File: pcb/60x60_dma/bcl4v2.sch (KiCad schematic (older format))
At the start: 31 parts, among them Q1 BSS138, SW1 SW_Push, SW2 SW_Push, SW3 SW_Push, U1 DS9166A-23, U2 STM32F070CBTx, Y1 Resonator

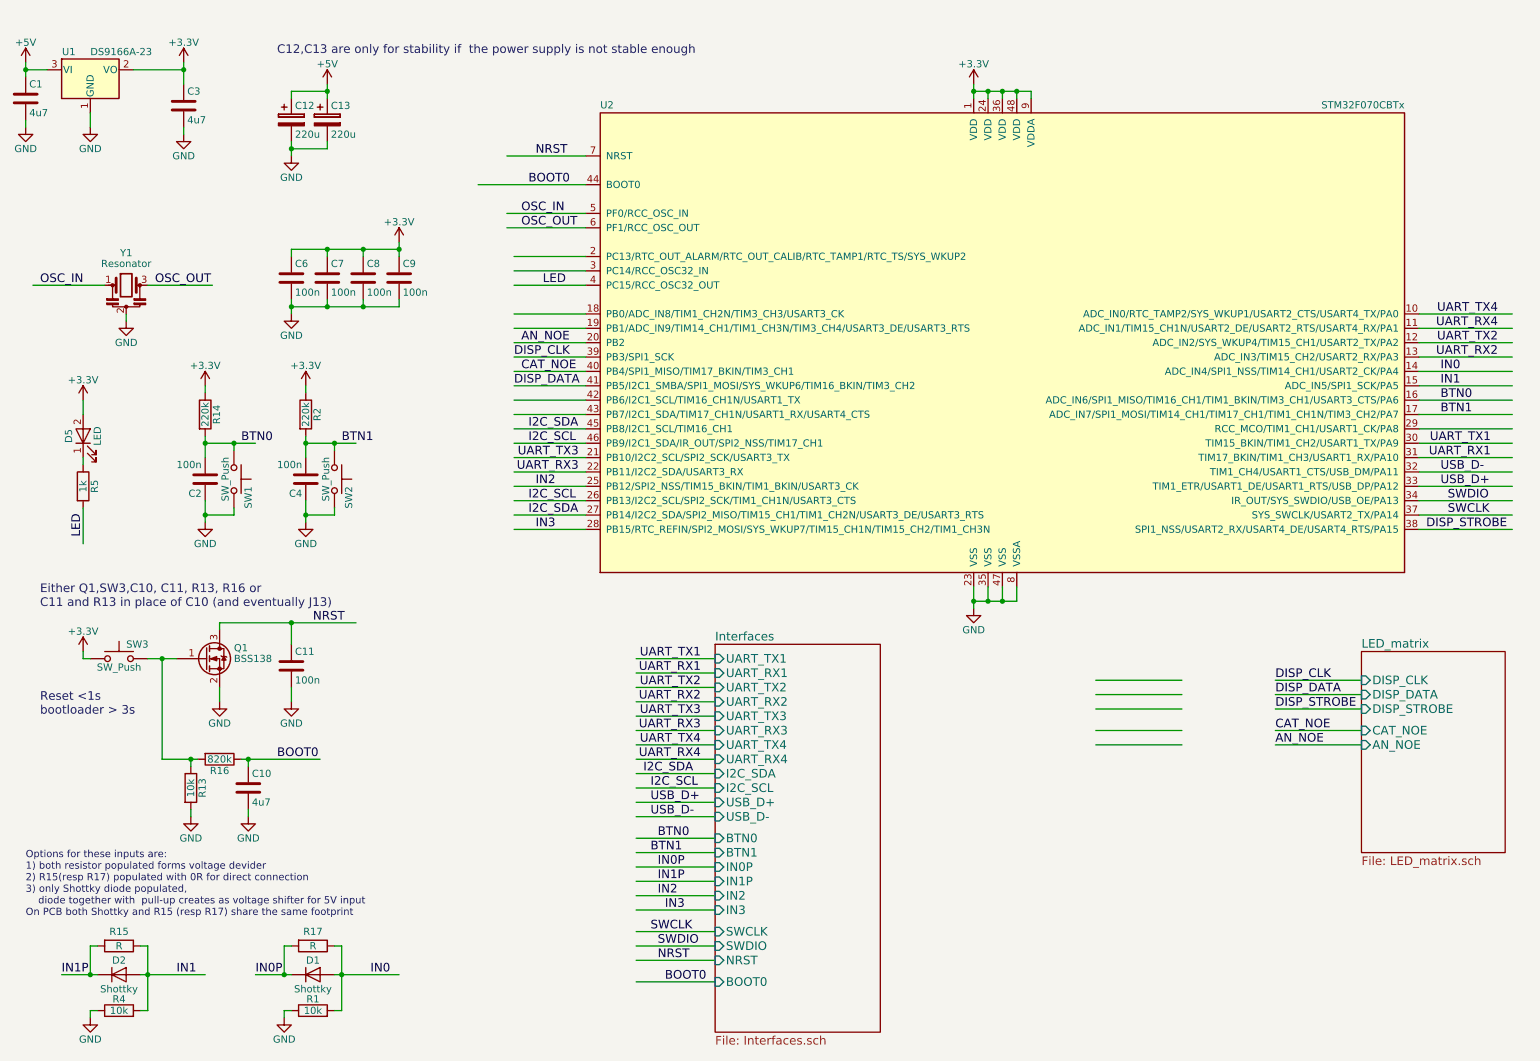
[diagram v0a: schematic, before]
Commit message: - add some testpoints
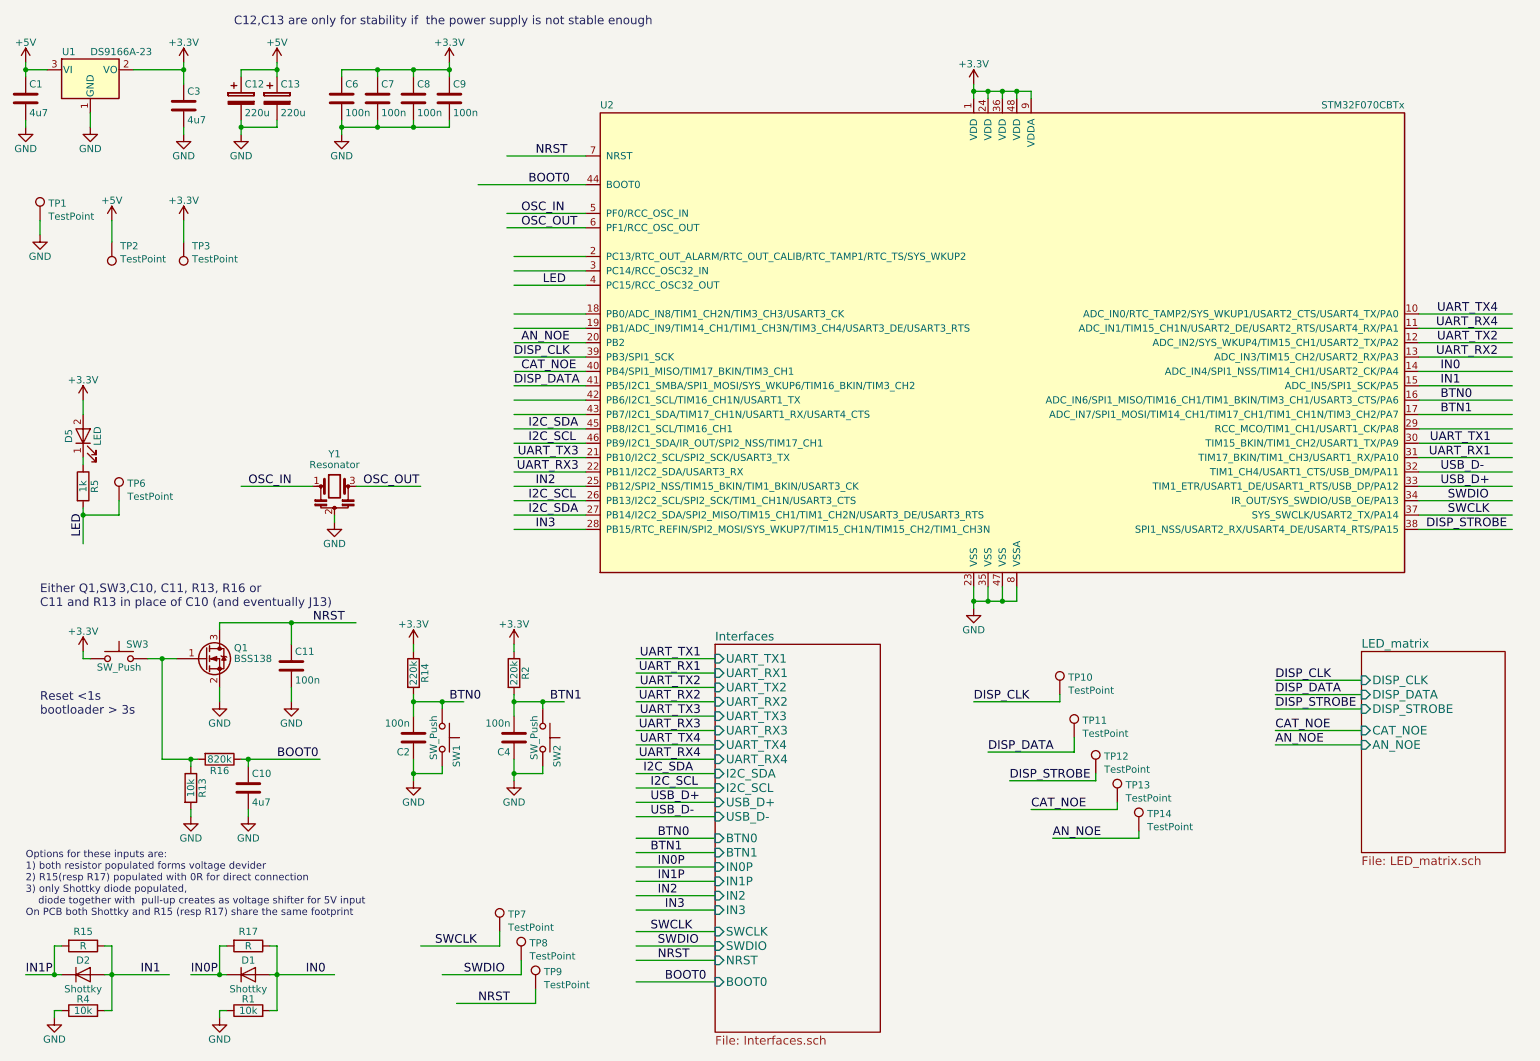
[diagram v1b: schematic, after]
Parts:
- added TP1, TP10, TP11, TP12, TP13, TP14, TP2, TP3, TP6, TP7, TP8, TP9: TestPoint, symbol Connector:TestPoint
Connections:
- wire segments 191 -> 208
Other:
- moved on the sheet: C12, C13, C2, C4, C6, C7, C8, C9, D1, D2, R1, R14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

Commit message: - fix display connections, add testpoints
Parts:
- removed TP7, TP8, TP9: TestPoint, symbol Connector:TestPoint
- TP1, TP10, TP11, TP12, TP13, TP14, TP2, TP3, TP6: footprint (none) -> TestPoint:TestPoint_Pad_D1.0mm
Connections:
- wire segments 208 -> 202
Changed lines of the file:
@@
 F 0 "TP1" H 858 2120 50  0000 L CNN
 F 1 "TestPoint" H 858 2029 50  0000 L CNN
-F 2 "" H 1000 2000 50  0001 C CNN
+F 2 "TestPoint:TestPoint_Pad_D1.0mm" H 1000 2000 50  0001 C CNN
 F 3 "~" H 1000 2000 50  0001 C CNN
 	1    800  2000
@@
 F 0 "TP2" H 1242 2177 50  0000 R CNN
 F 1 "TestPoint" H 1242 2268 50  0000 R CNN
-F 2 "" H 1500 2150 50  0001 C CNN
+F 2 "TestPoint:TestPoint_Pad_D1.0mm" H 1500 2150 50  0001 C CNN
 F 3 "~" H 1500 2150 50  0001 C CNN
 	1    1300 2150
@@
 F 0 "TP3" H 1742 2177 50  0000 R CNN
 F 1 "TestPoint" H 1742 2268 50  0000 R CNN
-F 2 "" H 2000 2150 50  0001 C CNN
+F 2 "TestPoint:TestPoint_Pad_D1.0mm" H 2000 2150 50  0001 C CNN
 F 3 "~" H 2000 2150 50  0001 C CNN
 	1    1800 2150
@@
 F 0 "TP6" H 1408 4070 50  0000 L CNN
 F 1 "TestPoint" H 1408 3979 50  0000 L CNN
-F 2 "" H 1550 3950 50  0001 C CNN
+F 2 "TestPoint:TestPoint_Pad_D1.0mm" H 1550 3950 50  0001 C CNN
 F 3 "~" H 1550 3950 50  0001 C CNN
 	1    1350 3950
@@
 F 0 "TP10" H 7958 5420 50  0000 L CNN
 F 1 "TestPoint" H 7958 5329 50  0000 L CNN
-F 2 "" H 8100 5300 50  0001 C CNN
+F 2 "TestPoint:TestPoint_Pad_D1.0mm" H 8100 5300 50  0001 C CNN
 F 3 "~" H 8100 5300 50  0001 C CNN
 	1    7900 5300
@@
 F 0 "TP11" H 8058 5720 50  0000 L CNN
 F 1 "TestPoint" H 8058 5629 50  0000 L CNN
-F 2 "" H 8200 5600 50  0001 C CNN
+F 2 "TestPoint:TestPoint_Pad_D1.0mm" H 8200 5600 50  0001 C CNN
 F 3 "~" H 8200 5600 50  0001 C CNN
 	1    8000 5600
@@
 F 0 "TP12" H 8208 5970 50  0000 L CNN
 F 1 "TestPoint" H 8208 5879 50  0000 L CNN
-F 2 "" H 8350 5850 50  0001 C CNN
+F 2 "TestPoint:TestPoint_Pad_D1.0mm" H 8350 5850 50  0001 C CNN
 F 3 "~" H 8350 5850 50  0001 C CNN
 	1    8150 5850
@@
 F 0 "TP13" H 8358 6170 50  0000 L CNN
 F 1 "TestPoint" H 8358 6079 50  0000 L CNN
-F 2 "" H 8500 6050 50  0001 C CNN
+F 2 "TestPoint:TestPoint_Pad_D1.0mm" H 8500 6050 50  0001 C CNN
 F 3 "~" H 8500 6050 50  0001 C CNN
 	1    8300 6050
@@
 F 0 "TP14" H 8508 6370 50  0000 L CNN
 F 1 "TestPoint" H 8508 6279 50  0000 L CNN
-F 2 "" H 8650 6250 50  0001 C CNN
+F 2 "TestPoint:TestPoint_Pad_D1.0mm" H 8650 6250 50  0001 C CNN
 F 3 "~" H 8650 6250 50  0001 C CNN
 	1    8450 6250
@@
 Wire Wire Line
 	8450 6250 8450 6300
-Text Label 3850 7450 0    60   ~ 0
-NRST
-Text Label 3750 7250 0    60   ~ 0
-SWDIO
-Text Label 3550 7050 0    60   ~ 0
-SWCLK
-Wire Wire Line
-	4000 7050 3450 7050
-Wire Wire Line
-	4150 7250 3600 7250
-Wire Wire Line
-	4250 7450 3700 7450
-$Comp
-L Connector:TestPoint TP7
-U 1 1 5C975F5F
-P 4000 6950
-F 0 "TP7" H 4058 7070 50  0000 L CNN
-F 1 "TestPoint" H 4058 6979 50  0000 L CNN
-F 2 "" H 4200 6950 50  0001 C CNN
-F 3 "~" H 4200 6950 50  0001 C CNN
-	1    4000 6950
-	1    0    0    -1
-$EndComp
-$Comp
-L Connector:TestPoint TP8
-U 1 1 5C98E363
-P 4150 7150
-F 0 "TP8" H 4208 7270 50  0000 L CNN
-F 1 "TestPoint" H 4208 7179 50  0000 L CNN
-F 2 "" H 4350 7150 50  0001 C CNN
-F 3 "~" H 4350 7150 50  0001 C CNN
-	1    4150 7150
-	1    0    0    -1
-$EndComp
-$Comp
-L Connector:TestPoint TP9
-U 1 1 5C98E423
-P 4250 7350
-F 0 "TP9" H 4308 7470 50  0000 L CNN
-F 1 "TestPoint" H 4308 7379 50  0000 L CNN
-F 2 "" H 4450 7350 50  0001 C CNN
-F 3 "~" H 4450 7350 50  0001 C CNN
-	1    4250 7350
-	1    0    0    -1
-$EndComp
-Wire Wire Line
-	4000 6950 4000 7050
-Wire Wire Line
-	4150 7150 4150 7250
-Wire Wire Line
-	4250 7350 4250 7450
 $EndSCHEMATC

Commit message: - add LSE crystal (needs to fix routing and zones)
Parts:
- added C14, C15: 2pF, kicad_lib:badger_C_0603_HandSoldering, symbol bcl4v2-rescue:C
- added Y2: ABS07-120-32.768kHz-T, kicad_lib:badger_crystal_ABS07-120-xx_handsolder, symbol Device:Crystal
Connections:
- net labels added: LSE_IN, LSE_OUT
- wire segments 202 -> 210
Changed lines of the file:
@@
 Text Label 1100 4200 1    60   ~ 0
 LED
-Text Label 4300 2450 0    60   ~ 0
+Text Label 4300 2250 0    60   ~ 0
 LED
 $Comp
@@
 Wire Wire Line
 	8450 6250 8450 6300
+$Comp
+L Device:Crystal Y2
+U 1 1 5C9B24E8
+P 2800 2850
+F 0 "Y2" H 2800 3118 50  0000 C CNN
+F 1 "ABS07-120-32.768kHz-T" H 2800 3027 50  0000 C CNN
+F 2 "kicad_lib:badger_crystal_ABS07-120-xx_handsolder" H 2800 2850 50  0001 C CNN
+F 3 "~" H 2800 2850 50  0001 C CNN
+	1    2800 2850
+	1    0    0    -1
+$EndComp
+$Comp
+L bcl4v2-rescue:C C14
+U 1 1 5C9B270E
+P 2550 3050
+F 0 "C14" H 2665 3096 50  0000 L CNN
+F 1 "2pF" H 2665 3005 50  0000 L CNN
+F 2 "kicad_lib:badger_C_0603_HandSoldering" H 2588 2900 50  0001 C CNN
+F 3 "" H 2550 3050 50  0001 C CNN
+	1    2550 3050
+	1    0    0    -1
+$EndComp
+$Comp
+L bcl4v2-rescue:GND #PWR028
+U 1 1 5C9B2815
+P 2550 3300
+F 0 "#PWR028" H 2550 3050 50  0001 C CNN
+F 1 "GND" H 2550 3150 50  0000 C CNN
+F 2 "" H 2550 3300 50  0001 C CNN
+F 3 "" H 2550 3300 50  0001 C CNN
+	1    2550 3300
+	1    0    0    -1
+$EndComp
+$Comp
+L bcl4v2-rescue:GND #PWR046
+U 1 1 5C9B2876
+P 3050 3300
+F 0 "#PWR046" H 3050 3050 50  0001 C CNN
+F 1 "GND" H 3050 3150 50  0000 C CNN
+F 2 "" H 3050 3300 50  0001 C CNN
+F 3 "" H 3050 3300 50  0001 C CNN
+	1    3050 3300
+	1    0    0    -1
+$EndComp
+Wire Wire Line
+	2650 2850 2550 2850
+Wire Wire Line
+	2550 2850 2550 2900
+Wire Wire Line
+	2950 2850 3050 2850
+Wire Wire Line
+	3050 2850 3050 2900
+Wire Wire Line
+	3050 2850 3400 2850
+Connection ~ 3050 2850
+Wire Wire Line
+	2550 2850 2050 2850
+Connection ~ 2550 2850
+Text Label 3150 2850 0    60   ~ 0
+LSE_OUT
+Text Label 2100 2850 0    60   ~ 0
+LSE_IN
+Text Label 4200 2350 0    60   ~ 0
+LSE_IN
+Text Label 4200 2450 0    60   ~ 0
+LSE_OUT
+Wire Wire Line
+	2550 3200 2550 3300
+Wire Wire Line
+	3050 3200 3050 3300
+$Comp
+L bcl4v2-rescue:C C15
+U 1 1 5C9FD7D5
+P 3050 3050
+F 0 "C15" H 3165 3096 50  0000 L CNN
+F 1 "2pF" H 3165 3005 50  0000 L CNN
+F 2 "kicad_lib:badger_C_0603_HandSoldering" H 3088 2900 50  0001 C CNN
+F 3 "" H 3050 3050 50  0001 C CNN
+	1    3050 3050
+	1    0    0    -1
+$EndComp
 $EndSCHEMATC

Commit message: - add OSHV logo, move LED a bit
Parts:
- D5: footprint LEDs:LED_0805_HandSoldering -> kicad_libraries_new:badger_LED_0805_HandSoldering
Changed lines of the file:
@@
 F 0 "D5" H 1100 3600 50  0000 C CNN
 F 1 "LED" H 1100 3400 50  0000 C CNN
-F 2 "LEDs:LED_0805_HandSoldering" H 1100 3500 50  0001 C CNN
+F 2 "kicad_libraries_new:badger_LED_0805_HandSoldering" H 1100 3500 50  0001 C CNN
 F 3 "" H 1100 3500 50  0001 C CNN
 	1    1100 3500

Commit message: - clense the schematics
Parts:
- added Q2: IRLML6402, kicad_libraries_new:badger_SOT-23_handsolder, symbol bcl4v2-rescue:Q_PMOS_GSD
- TP1: value TestPoint -> GND
- TP10: value TestPoint -> DCLK
- TP11: value TestPoint -> DDATA
- TP12: value TestPoint -> DSTRB
- TP13: value TestPoint -> CnOE
- TP14: value TestPoint -> AnOE
- TP2: value TestPoint -> +5V
- TP3: value TestPoint -> 3V3
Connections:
- net labels added: VCC
- wire segments 210 -> 213
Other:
- note added: "Auxiliary inputs, options for these inputs are:\n1) both resistor populated forms voltage devider\n2) R15(resp R17) populated with 0R for direct connection\n3) only Shottky diode populated, together with internal pull-up creates\n an input voltage level shifter (the pin can handle 5V input)\nOn PCB both Shottky and R15 (resp R17) share the same footprint\n"
- note added: "C12,C13 are only for stability if the power supply is not stable enough\nC6, C7, C8, C9 are for extra power stability in noisy environments"
- note added: "HW button debounce, It can\n be ommited , internal pull-up\nenabled and debounce\n can be done by SW."
- note added: "Reset <1s\nbootloader > 5s"
- note added: "The Q2 (P-MOSFET) is protection against wrong polarity of input.\nBut only in case that no power is applied to the USB.\nIt allows to powers the rail from the USB as well,\nbut once open by the USB power, there is no protection at all."
- note added: "Y1 is used for precise high speed\n clock, needed e.g. for USB"
- note added: "Y2 is used for low speed \nclock, needed e.g. for RTC"
- note removed: "C12,C13 are only for stability if the power supply is not stable enough"
- note removed: "Options for these inputs are:\n1) both resistor populated forms voltage devider\n2) R15(resp R17) populated with 0R for direct connection\n3) only Shottky diode populated, \n diode together with pull-up creates as voltage shifter for 5V input\nOn PCB both Shottky and R15 (resp R17) share the same footprint\n"
- note removed: "Reset <1s\nbootloader > 3s"
- moved on the sheet: C1, C10, C11, C12, C13, C14, C15, C2, C3, C4, C6, C7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
